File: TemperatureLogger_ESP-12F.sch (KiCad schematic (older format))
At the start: 19 parts, among them J1 Power for additional devices, J2 Additional I2C device, J3 Barrel_Jack, J4 FTDI_Cable, SW1 GND_to_reset, SW2 GND_to_program, U1 ESP-12F, U2 MCP1700-3302E_TO92, U6 GY-B11(BME-280)

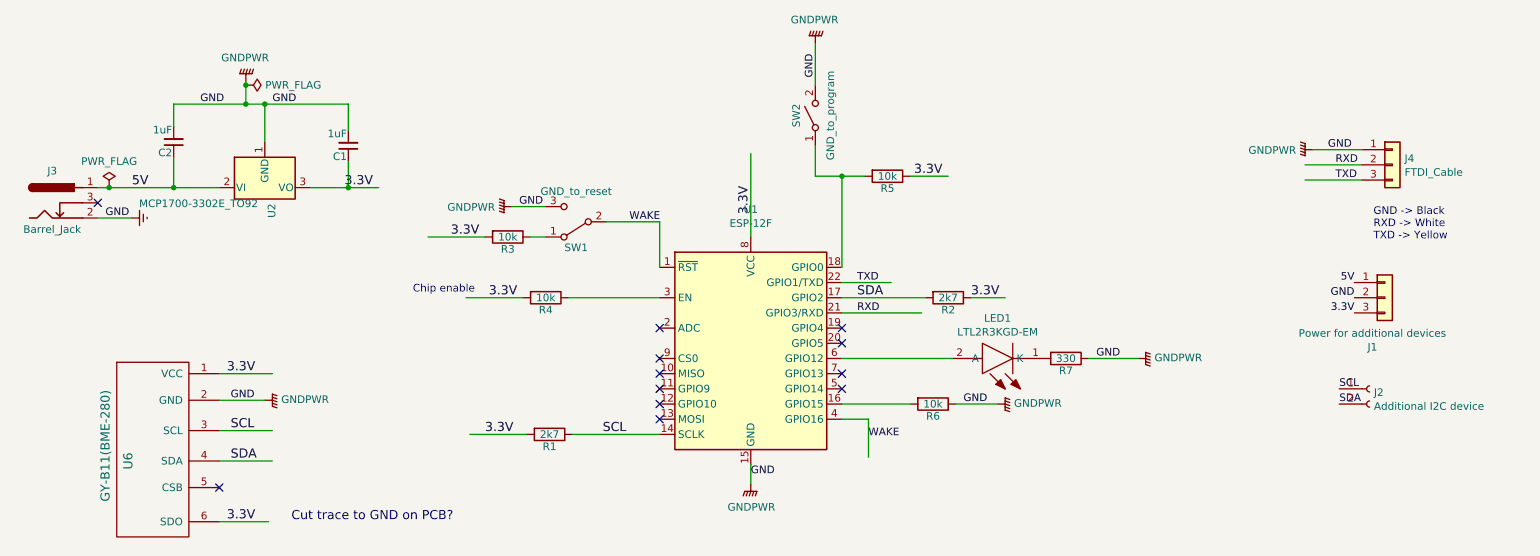
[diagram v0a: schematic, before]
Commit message: Adjusted BMP-280 footprint that was pointing to the wrong library
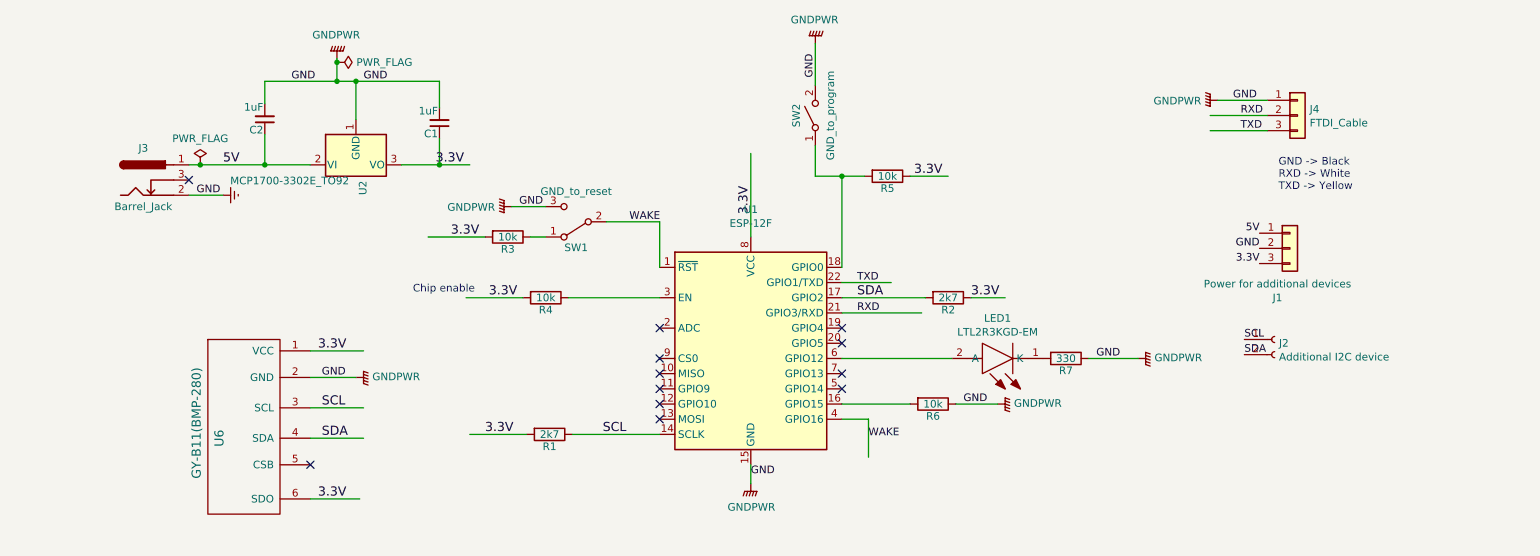
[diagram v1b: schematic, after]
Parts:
- U6: value GY-B11(BME-280) -> GY-B11(BMP-280); footprint ChickmaticPhase3-Simplify:GY-BME280-3.3 -> TemperatureLogger_ESP-12F:GY-BME280-3.3
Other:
- note removed: "Cut trace to GND on PCB?"
- moved on the sheet: C1, C2, J1, J2, J3, J4, U2, U6
